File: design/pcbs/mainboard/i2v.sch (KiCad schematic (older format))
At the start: 37 parts, among them U12 OPA1612AxD, U13 OPA1612AxD, U14 OPA1612AxD

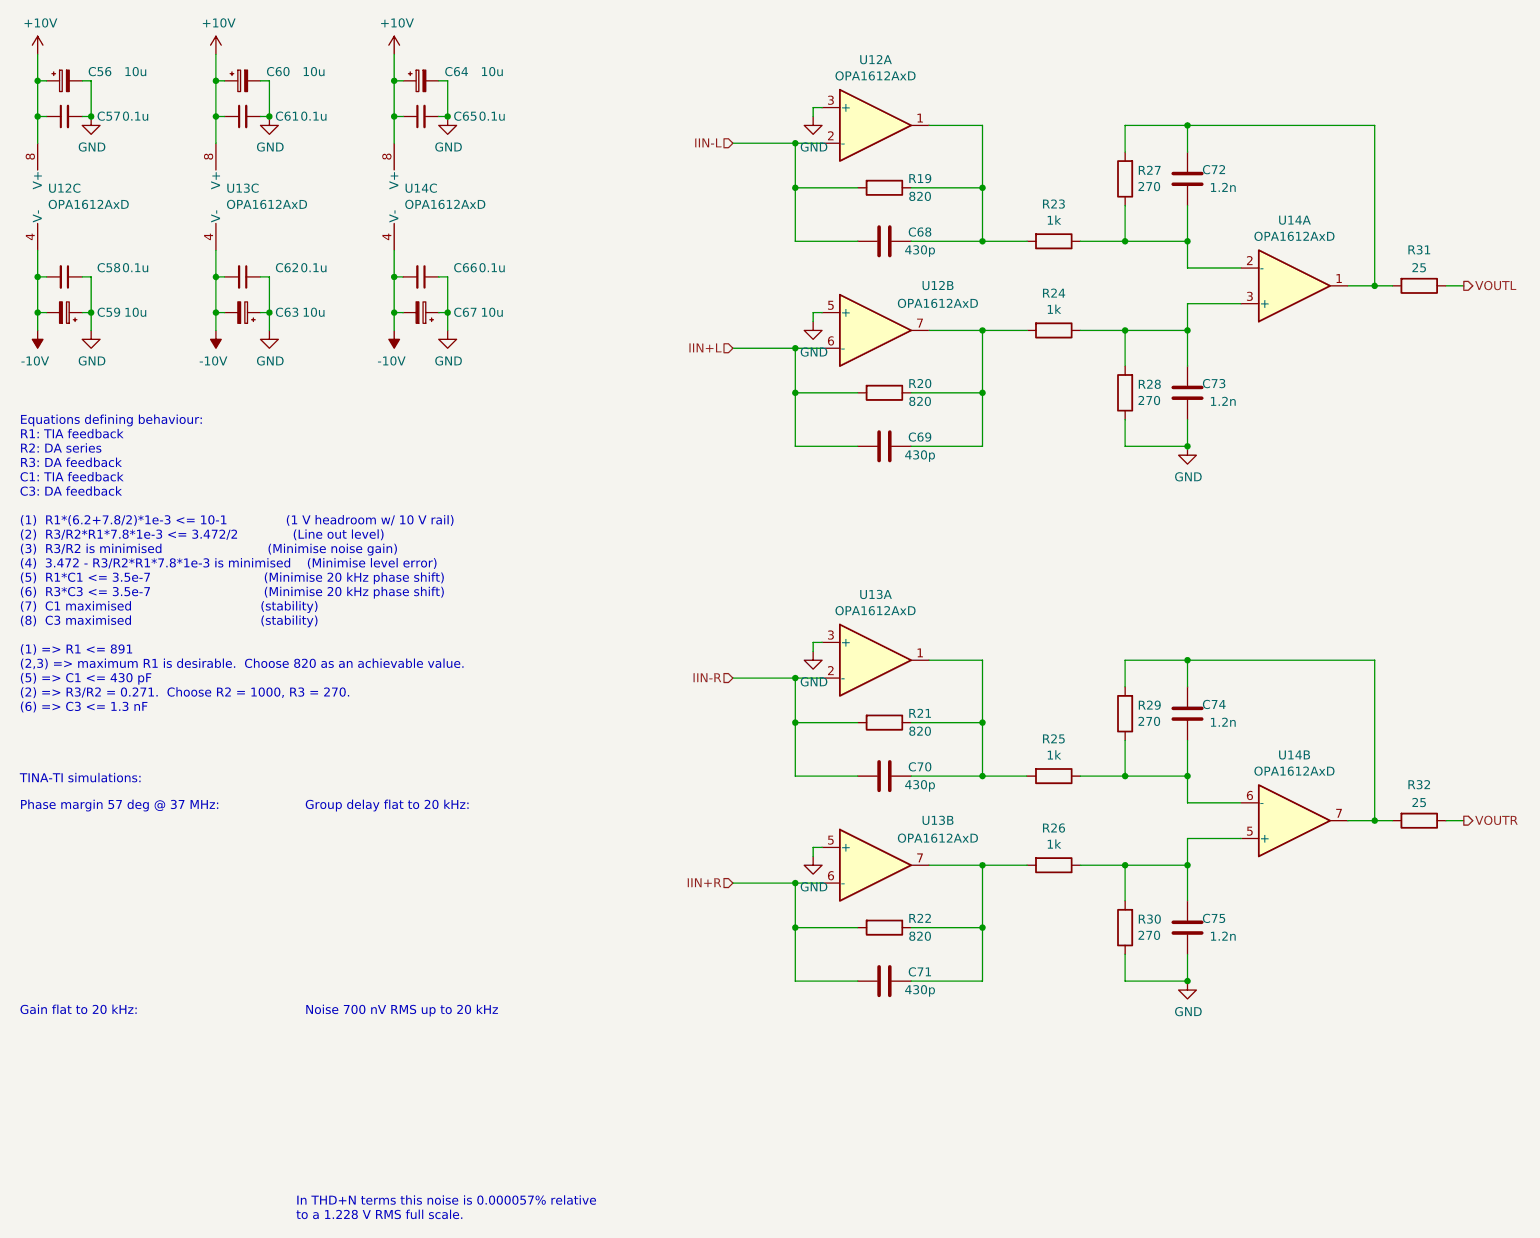
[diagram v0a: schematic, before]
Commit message: Renumbered footprints to follow board position.
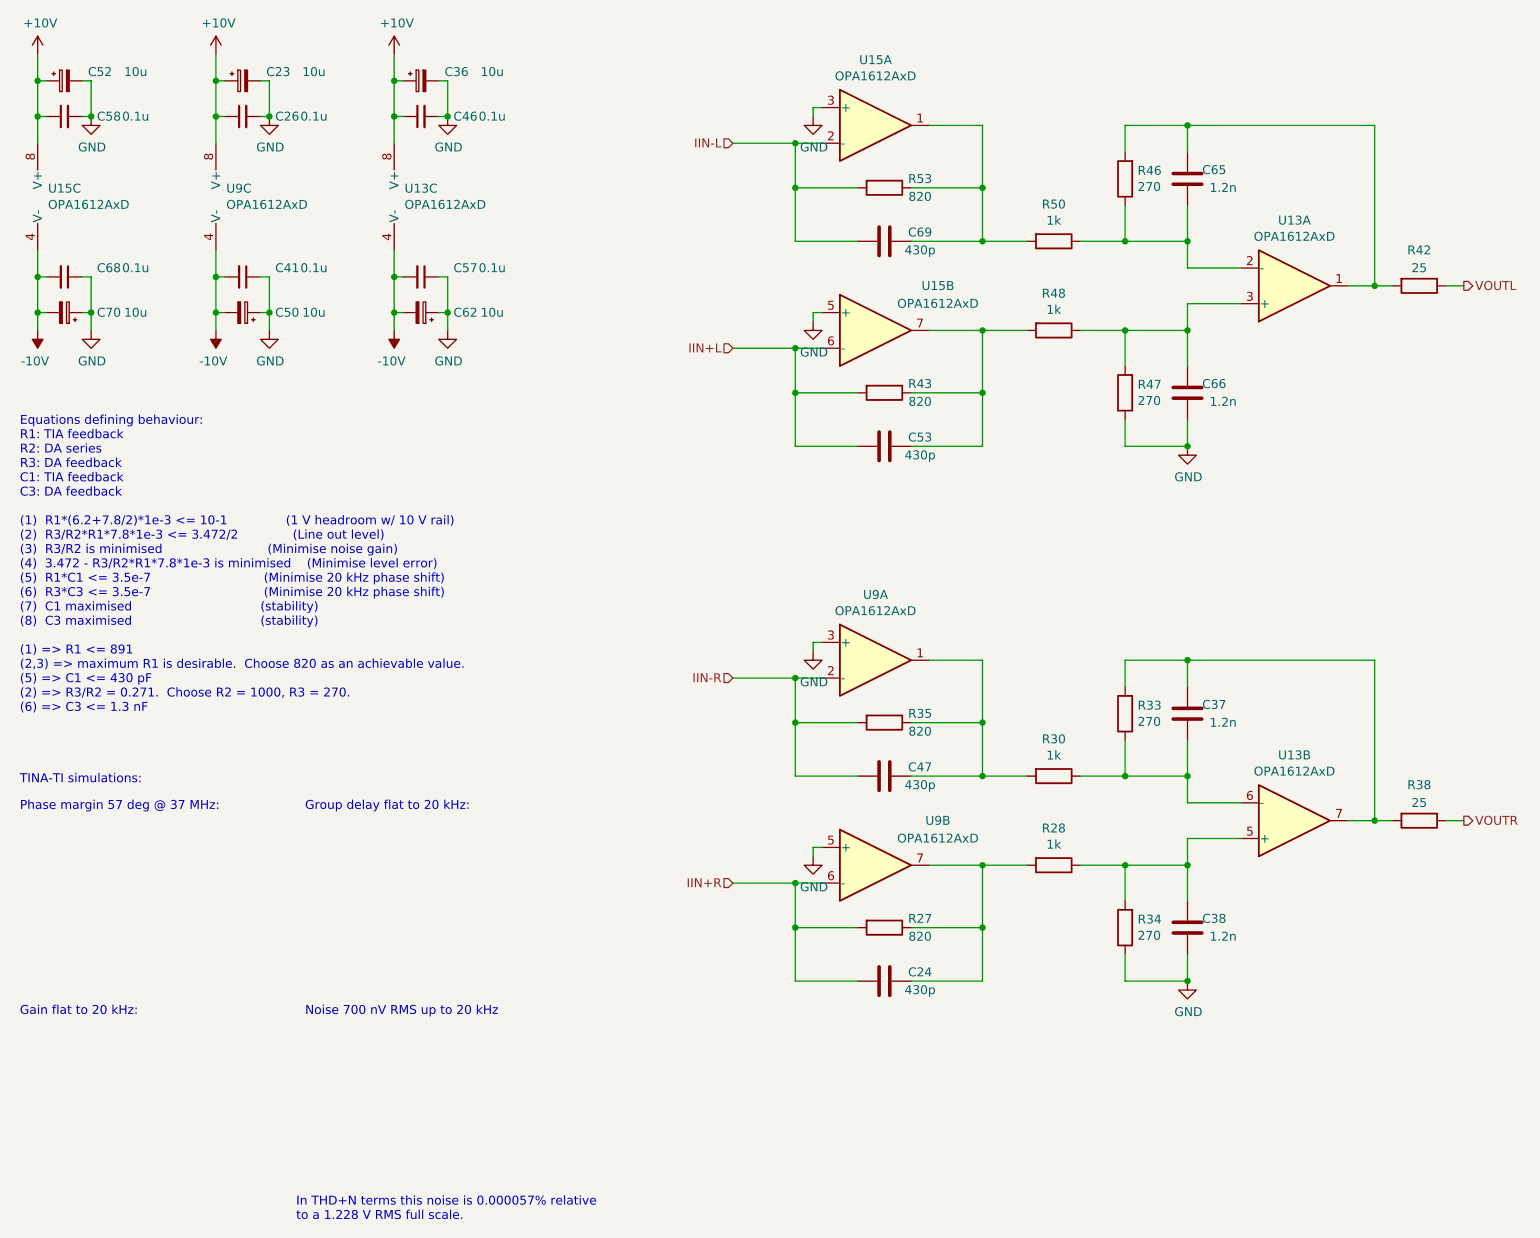
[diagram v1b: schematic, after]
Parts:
- renumbered C60 to C23, C71 to C24, C61 to C26, C64 to C36, C74 to C37, C75 to C38, C62 to C41, C65 to C46, C70 to C47, C63 to C50, C56 to C52, C69 to C53, C66 to C57, C57 to C58, C67 to C62, C72 to C65, C73 to C66, C58 to C68, C68 to C69, C59 to C70, R22 to R27, R26 to R28, R25 to R30, R29 to R33, R30 to R34, R21 to R35, R32 to R38, R31 to R42, R20 to R43, R27 to R46, R28 to R47, R24 to R48, R23 to R50, R19 to R53, U14 to U13, U12 to U15, U13 to U9

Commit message: Fixed title blocks. Added fab outputs.
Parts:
- U13, U15, U9: LCSC (none) -> C94590
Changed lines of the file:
@@
 encoding utf-8
 Sheet 7 10
-Title ""
-Date ""
-Rev ""
-Comp ""
-Comment1 ""
-Comment2 ""
+Title "DAC1 Main board"
+Date "2020-06-27"
+Rev "1.0.0"
+Comp "© Mark Pinese 2020"
+Comment1 "To view a copy of this license, visit https://creativecommons.org/licenses/by/4.0"
+Comment2 "This work is licensed under CC BY 4.0."
 Comment3 ""
 Comment4 ""
@@
 F 4 "296-39098-1-ND" H 1100 1600 50  0001 C CNN "DigiKey"
 F 5 "Yes" H 1100 1600 50  0001 C CNN "Done"
+F 6 "C94590" H 1100 1600 50  0001 C CNN "LCSC"
 	3    1100 1600
 	1    0    0    -1
@@
 F 4 "296-39098-1-ND" H 2100 1600 50  0001 C CNN "DigiKey"
 F 5 "Yes" H 2100 1600 50  0001 C CNN "Done"
+F 6 "C94590" H 2100 1600 50  0001 C CNN "LCSC"
 	3    2100 1600
 	1    0    0    -1
@@
 F 4 "296-39098-1-ND" H 5700 4200 50  0001 C CNN "DigiKey"
 F 5 "Yes" H 5700 4200 50  0001 C CNN "Done"
+F 6 "C94590" H 5700 4200 50  0001 C CNN "LCSC"
 	1    5700 4200
 	1    0    0    -1
@@
 F 4 "296-39098-1-ND" H 5700 5350 50  0001 C CNN "DigiKey"
 F 5 "Yes" H 5700 5350 50  0001 C CNN "Done"
+F 6 "C94590" H 5700 5350 50  0001 C CNN "LCSC"
 	2    5700 5350
 	1    0    0    -1
@@
 F 4 "296-39098-1-ND" H 8050 5100 50  0001 C CNN "DigiKey"
 F 5 "Yes" H 8050 5100 50  0001 C CNN "Done"
+F 6 "C94590" H 8050 5100 50  0001 C CNN "LCSC"
 	2    8050 5100
 	1    0    0    1
@@
 F 4 "296-39098-1-ND" H 3100 1600 50  0001 C CNN "DigiKey"
 F 5 "Yes" H 3100 1600 50  0001 C CNN "Done"
+F 6 "C94590" H 3100 1600 50  0001 C CNN "LCSC"
 	3    3100 1600
 	1    0    0    -1
@@
 F 4 "296-39098-1-ND" H 5700 1200 50  0001 C CNN "DigiKey"
 F 5 "Yes" H 5700 1200 50  0001 C CNN "Done"
+F 6 "C94590" H 5700 1200 50  0001 C CNN "LCSC"
 	1    5700 1200
 	1    0    0    -1
@@
 F 4 "296-39098-1-ND" H 5700 2350 50  0001 C CNN "DigiKey"
 F 5 "Yes" H 5700 2350 50  0001 C CNN "Done"
+F 6 "C94590" H 5700 2350 50  0001 C CNN "LCSC"
 	2    5700 2350
 	1    0    0    -1
@@
 F 4 "296-39098-1-ND" H 8050 2100 50  0001 C CNN "DigiKey"
 F 5 "Yes" H 8050 2100 50  0001 C CNN "Done"
+F 6 "C94590" H 8050 2100 50  0001 C CNN "LCSC"
 	1    8050 2100
 	1    0    0    1
